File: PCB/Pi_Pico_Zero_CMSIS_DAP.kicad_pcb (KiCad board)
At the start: 2 copper layers, 24 x 37.5 mm, 8 parts, among them J1 CONN_PROG, J2 CONN_UART, U1 Pi_Pico_Zero

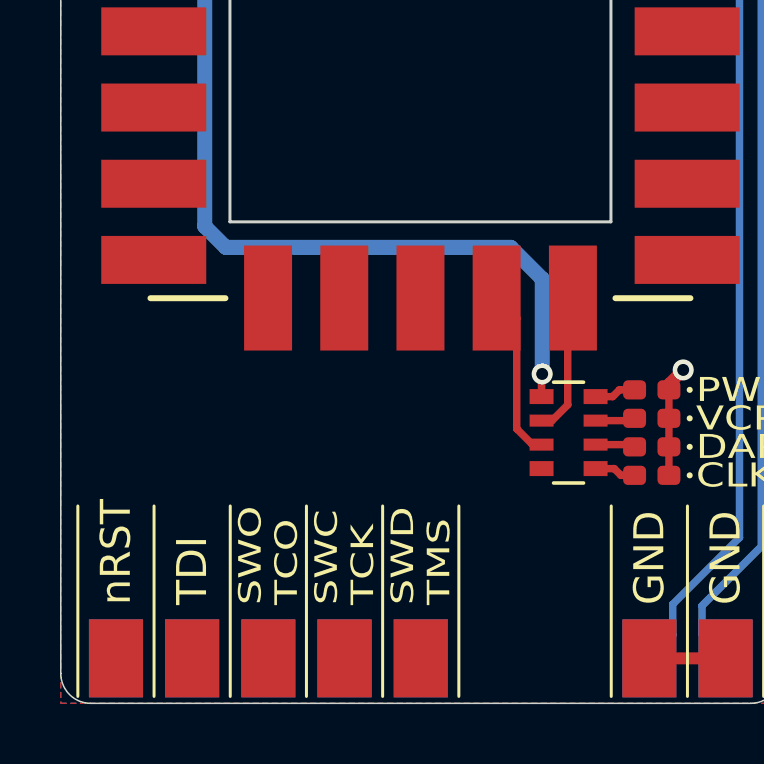
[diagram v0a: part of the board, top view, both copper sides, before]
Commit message: Restructured file tree
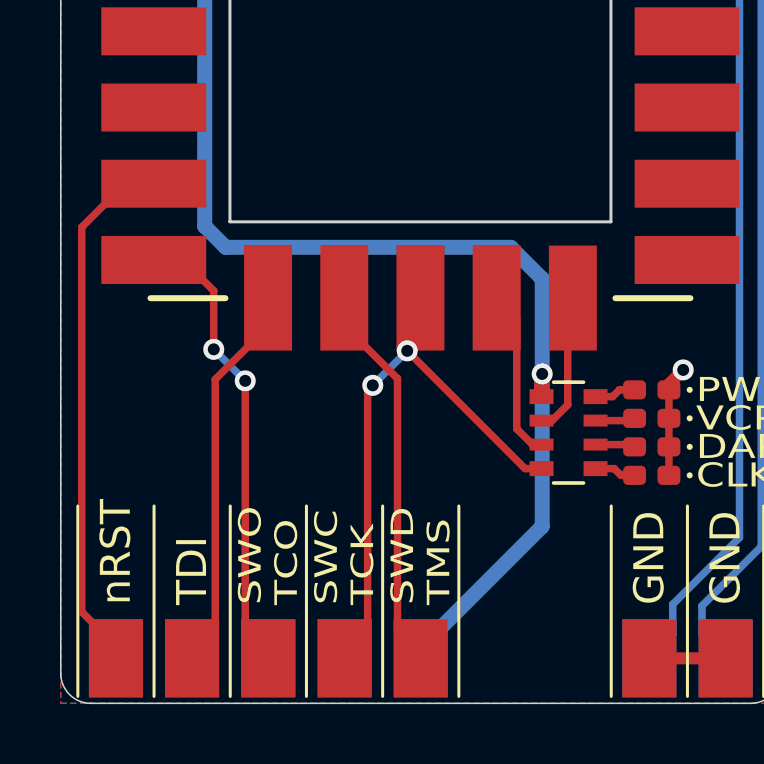
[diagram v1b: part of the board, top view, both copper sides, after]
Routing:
- net /SWC/TCK: track 0.13 -> 19.3 mm, vias 0 -> 2
- net /nRESET: track 0.00 -> 17.8 mm
- net /SWO/TDO: track 0.00 -> 15.4 mm, vias 0 -> 2
- net /SWD/TMS: track 0.00 -> 13.1 mm
- net /TDI: track 0.00 -> 13.1 mm
- net /3V3: track 31.7 -> 42.9 mm

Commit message: MkI PCB Final
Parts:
- moved D1 48.3 mm to (142.3, 89.7)
- moved D2 48.3 mm to (142.3, 90.7)
- moved D3 48.3 mm to (142.3, 91.6)
- moved D4 48.3 mm to (142.3, 92.5)
- moved RN1 48.3 mm to (139.6, 91.1)
- moved U1 48.3 mm to (134.6, 75.1)
- moved J1 48.3 mm to (134.6, 98.7)
- moved J2 48.3 mm to (142.3, 98.7)
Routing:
- net GND: track 6.25 -> 12.8 mm, vias 1 -> 23
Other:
- board text added: "Pi Pico Zero CMSIS-DAP MkI Nov 2024"
- board text removed: "1.2mm?"
